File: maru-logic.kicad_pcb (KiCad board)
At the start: 2 copper layers, 182.9 x 111.8 mm, 190 parts, among them J1 USB-C, Q1 MMBT3904, Q10 MMBT3904, Q11 MMBT3904, Q12 MMBT3904, Q2 MMBT3904, Q3 MMBT3904, Q4 MMBT3904, Q5 MMBT3904, Q6 MMBT3904, Q7 MMBT3904, Q8 MMBT3904, Q9 MMBT3904, SW1 Push, SW2 Push, SW3 Push, SW4 Push, SW5 Push, SW6 Push, SW7 Push, U1 4011, U10 4011, U11 4011, U2 4011, U3 4011, U4 4011, U5 4011, U6 4011, U7 4011, U8 4011, U9 4011

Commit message: routing done
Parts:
- added C12: 100n, Capacitor_SMD:C_0402_1005Metric, F.Cu at (48.9, 76.8)
- added C3: 100n, Capacitor_SMD:C_0402_1005Metric, F.Cu at (79.5, 93.5)
- added C6: 100n, Capacitor_SMD:C_0402_1005Metric, F.Cu at (79.5, 69.6)
- added C9: 100n, Capacitor_SMD:C_0402_1005Metric, F.Cu at (79.5, 45.2)
- SW1, SW2, SW3, SW4, SW5, SW6, SW7: footprint mark:BUTTON_XKB_TS-1187A-B-A-B_C318884 -> mark:jlc_pushbutton_wrong_model
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- renumbered C8 to C10, C9 to C11, C2 to C13, C10 to C14, C11 to C15, C12 to C16, C13 to C17, C14 to C18, C15 to C19, C3 to C2, C6 to C7, C7 to C8, Q3 to Q1, Q7 to Q10, Q8 to Q11, Q10 to Q12, Q6 to Q2, Q9 to Q3, Q11 to Q4, Q12 to Q5, Q1 to Q6, Q2 to Q7, Q4 to Q8, Q5 to Q9, R2 to R1, R15 to R10, R16 to R11, R17 to R12, R25 to R13, R26 to R14, R27 to R15, R28 to R16, R29 to R17, R30 to R18, R43 to R19, R3 to R2, R44 to R20, R45 to R21, R46 to R22, R47 to R23, R48 to R24, R61 to R25, R62 to R26, R63 to R27, R64 to R28, R65 to R29, R1 to R3, R66 to R30, R73 to R31, R74 to R32, R75 to R33, R76 to R34, R77 to R35, R78 to R36, R79 to R37, R80 to R38, R81 to R39, R9 to R4, R82 to R40, R83 to R41, R84 to R42, R4 to R43, R5 to R44, R6 to R45, R7 to R46, R8 to R47, R18 to R48, R19 to R49, R10 to R5, R20 to R50, R21 to R51, R22 to R52, R23 to R53, R24 to R54, R31 to R55, R32 to R56, R33 to R57, R34 to R58, R35 to R59, R11 to R6, R36 to R60, R37 to R61, R38 to R62, R39 to R63, R40 to R64, R41 to R65, R42 to R66, R49 to R67, R50 to R68, R51 to R69, R12 to R7, R52 to R70, R53 to R71, R54 to R72, R55 to R73, R56 to R74, R57 to R75, R58 to R76, R59 to R77, R60 to R78, R67 to R79, R13 to R8, R68 to R80, R69 to R81, R70 to R82, R71 to R83, R72 to R84, R14 to R9, U3 to U2, U2 to U3, U5 to U4, U4 to U5
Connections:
- D1 pad 1: /Toggle Button 1/LEDs 1/LED drivers/LED1 -> /Output LEDs/LED_AND_X/LED array x5/LED1
- D10 pad 1: /Toggle Button 2/LEDs 1/LED drivers/LED5 -> /Output LEDs/LED_OR_X/LED array x5/LED5
- D11 pad 1: /Output LEDs/LED_AND_X/LED drivers/LED1 -> /Output LEDs/LED_XOR_X/LED array x5/LED1
- D12 pad 1: /Output LEDs/LED_AND_X/LED drivers/LED2 -> /Output LEDs/LED_XOR_X/LED array x5/LED2
- D13 pad 1: /Output LEDs/LED_AND_X/LED drivers/LED3 -> /Output LEDs/LED_XOR_X/LED array x5/LED3
- D14 pad 1: /Output LEDs/LED_AND_X/LED drivers/LED4 -> /Output LEDs/LED_XOR_X/LED array x5/LED4
- D15 pad 1: /Output LEDs/LED_AND_X/LED drivers/LED5 -> /Output LEDs/LED_XOR_X/LED array x5/LED5
- D16 pad 1: /Toggle Button 3/LEDs 1/LED drivers/LED1 -> /Output LEDs/LED_NOT_X/LED array x5/LED1
- D17 pad 1: /Toggle Button 3/LEDs 1/LED drivers/LED2 -> /Output LEDs/LED_NOT_X/LED array x5/LED2
- D18 pad 1: /Toggle Button 3/LEDs 1/LED drivers/LED3 -> /Output LEDs/LED_NOT_X/LED array x5/LED3
- D19 pad 1: /Toggle Button 3/LEDs 1/LED drivers/LED4 -> /Output LEDs/LED_NOT_X/LED array x5/LED4
- D2 pad 1: /Toggle Button 1/LEDs 1/LED drivers/LED2 -> /Output LEDs/LED_AND_X/LED array x5/LED2
- D20 pad 1: /Toggle Button 3/LEDs 1/LED drivers/LED5 -> /Output LEDs/LED_NOT_X/LED array x5/LED5
- D21 pad 1: /Toggle Button 4/LEDs 1/LED drivers/LED1 -> /Output LEDs/LED_ALL_X/LED array x5/LED1
- D22 pad 1: /Toggle Button 4/LEDs 1/LED drivers/LED2 -> /Output LEDs/LED_ALL_X/LED array x5/LED2
- D23 pad 1: /Toggle Button 4/LEDs 1/LED drivers/LED3 -> /Output LEDs/LED_ALL_X/LED array x5/LED3
- D24 pad 1: /Toggle Button 4/LEDs 1/LED drivers/LED4 -> /Output LEDs/LED_ALL_X/LED array x5/LED4
- D25 pad 1: /Toggle Button 4/LEDs 1/LED drivers/LED5 -> /Output LEDs/LED_ALL_X/LED array x5/LED5
- D26 pad 1: /Output LEDs/LED_OR_X/LED drivers/LED1 -> /Toggle Button 1/LEDs 1/LED array x5/LED1
- D27 pad 1: /Output LEDs/LED_OR_X/LED drivers/LED2 -> /Toggle Button 1/LEDs 1/LED array x5/LED2
- D28 pad 1: /Output LEDs/LED_OR_X/LED drivers/LED3 -> /Toggle Button 1/LEDs 1/LED array x5/LED3
- D29 pad 1: /Output LEDs/LED_OR_X/LED drivers/LED4 -> /Toggle Button 1/LEDs 1/LED array x5/LED4
- D3 pad 1: /Toggle Button 1/LEDs 1/LED drivers/LED3 -> /Output LEDs/LED_AND_X/LED array x5/LED3
- D30 pad 1: /Output LEDs/LED_OR_X/LED drivers/LED5 -> /Toggle Button 1/LEDs 1/LED array x5/LED5
- D31 pad 1: /Toggle Button 5/LEDs 1/LED drivers/LED1 -> /Toggle Button 2/LEDs 1/LED array x5/LED1
- D32 pad 1: /Toggle Button 5/LEDs 1/LED drivers/LED2 -> /Toggle Button 2/LEDs 1/LED array x5/LED2
- D33 pad 1: /Toggle Button 5/LEDs 1/LED drivers/LED3 -> /Toggle Button 2/LEDs 1/LED array x5/LED3
- D34 pad 1: /Toggle Button 5/LEDs 1/LED drivers/LED4 -> /Toggle Button 2/LEDs 1/LED array x5/LED4
- D35 pad 1: /Toggle Button 5/LEDs 1/LED drivers/LED5 -> /Toggle Button 2/LEDs 1/LED array x5/LED5
- D36 pad 1: /Toggle Button 6/LEDs 1/LED drivers/LED1 -> /Toggle Button 3/LEDs 1/LED array x5/LED1
- D37 pad 1: /Toggle Button 6/LEDs 1/LED drivers/LED2 -> /Toggle Button 3/LEDs 1/LED array x5/LED2
- D38 pad 1: /Toggle Button 6/LEDs 1/LED drivers/LED3 -> /Toggle Button 3/LEDs 1/LED array x5/LED3
- D39 pad 1: /Toggle Button 6/LEDs 1/LED drivers/LED4 -> /Toggle Button 3/LEDs 1/LED array x5/LED4
- D4 pad 1: /Toggle Button 1/LEDs 1/LED drivers/LED4 -> /Output LEDs/LED_AND_X/LED array x5/LED4
- D40 pad 1: /Toggle Button 6/LEDs 1/LED drivers/LED5 -> /Toggle Button 3/LEDs 1/LED array x5/LED5
- D41 pad 1: /Output LEDs/LED_XOR_X/LED drivers/LED1 -> /Toggle Button 4/LEDs 1/LED array x5/LED1
- D42 pad 1: /Output LEDs/LED_XOR_X/LED drivers/LED2 -> /Toggle Button 4/LEDs 1/LED array x5/LED2
- D43 pad 1: /Output LEDs/LED_XOR_X/LED drivers/LED3 -> /Toggle Button 4/LEDs 1/LED array x5/LED3
- D44 pad 1: /Output LEDs/LED_XOR_X/LED drivers/LED4 -> /Toggle Button 4/LEDs 1/LED array x5/LED4
- D45 pad 1: /Output LEDs/LED_XOR_X/LED drivers/LED5 -> /Toggle Button 4/LEDs 1/LED array x5/LED5
- D46 pad 1: /Toggle Button 7/LEDs 1/LED drivers/LED1 -> /Toggle Button 5/LEDs 1/LED array x5/LED1
- D47 pad 1: /Toggle Button 7/LEDs 1/LED drivers/LED2 -> /Toggle Button 5/LEDs 1/LED array x5/LED2
- D48 pad 1: /Toggle Button 7/LEDs 1/LED drivers/LED3 -> /Toggle Button 5/LEDs 1/LED array x5/LED3
- D49 pad 1: /Toggle Button 7/LEDs 1/LED drivers/LED4 -> /Toggle Button 5/LEDs 1/LED array x5/LED4
- D5 pad 1: /Toggle Button 1/LEDs 1/LED drivers/LED5 -> /Output LEDs/LED_AND_X/LED array x5/LED5
- D50 pad 1: /Toggle Button 7/LEDs 1/LED drivers/LED5 -> /Toggle Button 5/LEDs 1/LED array x5/LED5
- D51 pad 1: /Output LEDs/LED_NOT_X/LED drivers/LED1 -> /Toggle Button 6/LEDs 1/LED array x5/LED1
- D52 pad 1: /Output LEDs/LED_NOT_X/LED drivers/LED2 -> /Toggle Button 6/LEDs 1/LED array x5/LED2
- D53 pad 1: /Output LEDs/LED_NOT_X/LED drivers/LED3 -> /Toggle Button 6/LEDs 1/LED array x5/LED3
- D54 pad 1: /Output LEDs/LED_NOT_X/LED drivers/LED4 -> /Toggle Button 6/LEDs 1/LED array x5/LED4
- D55 pad 1: /Output LEDs/LED_NOT_X/LED drivers/LED5 -> /Toggle Button 6/LEDs 1/LED array x5/LED5
- D56 pad 1: /Output LEDs/LED_ALL_X/LED drivers/LED1 -> /Toggle Button 7/LEDs 1/LED array x5/LED1
- D57 pad 1: /Output LEDs/LED_ALL_X/LED drivers/LED2 -> /Toggle Button 7/LEDs 1/LED array x5/LED2
- D58 pad 1: /Output LEDs/LED_ALL_X/LED drivers/LED3 -> /Toggle Button 7/LEDs 1/LED array x5/LED3
- D59 pad 1: /Output LEDs/LED_ALL_X/LED drivers/LED4 -> /Toggle Button 7/LEDs 1/LED array x5/LED4
- D6 pad 1: /Toggle Button 2/LEDs 1/LED drivers/LED1 -> /Output LEDs/LED_OR_X/LED array x5/LED1
- D60 pad 1: /Output LEDs/LED_ALL_X/LED drivers/LED5 -> /Toggle Button 7/LEDs 1/LED array x5/LED5
- D7 pad 1: /Toggle Button 2/LEDs 1/LED drivers/LED2 -> /Output LEDs/LED_OR_X/LED array x5/LED2
- D8 pad 1: /Toggle Button 2/LEDs 1/LED drivers/LED3 -> /Output LEDs/LED_OR_X/LED array x5/LED3
- D9 pad 1: /Toggle Button 2/LEDs 1/LED drivers/LED4 -> /Output LEDs/LED_OR_X/LED array x5/LED4
- R14 pad 1: /Output LEDs/LED_AND_X/LED drivers/LED1 -> /Output LEDs/LED_AND_X/LED array x5/LED1
- R15 pad 1: /Output LEDs/LED_AND_X/LED drivers/LED2 -> /Output LEDs/LED_AND_X/LED array x5/LED2
- R16 pad 1: /Output LEDs/LED_AND_X/LED drivers/LED3 -> /Output LEDs/LED_AND_X/LED array x5/LED3
- R17 pad 1: /Output LEDs/LED_AND_X/LED drivers/LED4 -> /Output LEDs/LED_AND_X/LED array x5/LED4
- R18 pad 1: /Output LEDs/LED_AND_X/LED drivers/LED5 -> /Output LEDs/LED_AND_X/LED array x5/LED5
- R20 pad 1: /Output LEDs/LED_OR_X/LED drivers/LED1 -> /Output LEDs/LED_OR_X/LED array x5/LED1
- R21 pad 1: /Output LEDs/LED_OR_X/LED drivers/LED2 -> /Output LEDs/LED_OR_X/LED array x5/LED2
- R22 pad 1: /Output LEDs/LED_OR_X/LED drivers/LED3 -> /Output LEDs/LED_OR_X/LED array x5/LED3
- R23 pad 1: /Output LEDs/LED_OR_X/LED drivers/LED4 -> /Output LEDs/LED_OR_X/LED array x5/LED4
- R24 pad 1: /Output LEDs/LED_OR_X/LED drivers/LED5 -> /Output LEDs/LED_OR_X/LED array x5/LED5
- R26 pad 1: /Output LEDs/LED_XOR_X/LED drivers/LED1 -> /Output LEDs/LED_XOR_X/LED array x5/LED1
- R27 pad 1: /Output LEDs/LED_XOR_X/LED drivers/LED2 -> /Output LEDs/LED_XOR_X/LED array x5/LED2
- R28 pad 1: /Output LEDs/LED_XOR_X/LED drivers/LED3 -> /Output LEDs/LED_XOR_X/LED array x5/LED3
- R29 pad 1: /Output LEDs/LED_XOR_X/LED drivers/LED4 -> /Output LEDs/LED_XOR_X/LED array x5/LED4
- R30 pad 1: /Output LEDs/LED_XOR_X/LED drivers/LED5 -> /Output LEDs/LED_XOR_X/LED array x5/LED5
- R32 pad 1: /Output LEDs/LED_NOT_X/LED drivers/LED1 -> /Output LEDs/LED_NOT_X/LED array x5/LED1
- R33 pad 1: /Output LEDs/LED_NOT_X/LED drivers/LED2 -> /Output LEDs/LED_NOT_X/LED array x5/LED2
- R34 pad 1: /Output LEDs/LED_NOT_X/LED drivers/LED3 -> /Output LEDs/LED_NOT_X/LED array x5/LED3
- R35 pad 1: /Output LEDs/LED_NOT_X/LED drivers/LED4 -> /Output LEDs/LED_NOT_X/LED array x5/LED4
- R36 pad 1: /Output LEDs/LED_NOT_X/LED drivers/LED5 -> /Output LEDs/LED_NOT_X/LED array x5/LED5
- R38 pad 1: /Output LEDs/LED_ALL_X/LED drivers/LED1 -> /Output LEDs/LED_ALL_X/LED array x5/LED1
- R39 pad 1: /Output LEDs/LED_ALL_X/LED drivers/LED2 -> /Output LEDs/LED_ALL_X/LED array x5/LED2
- R40 pad 1: /Output LEDs/LED_ALL_X/LED drivers/LED3 -> /Output LEDs/LED_ALL_X/LED array x5/LED3
- R41 pad 1: /Output LEDs/LED_ALL_X/LED drivers/LED4 -> /Output LEDs/LED_ALL_X/LED array x5/LED4
- R42 pad 1: /Output LEDs/LED_ALL_X/LED drivers/LED5 -> /Output LEDs/LED_ALL_X/LED array x5/LED5
- R44 pad 1: /Toggle Button 1/LEDs 1/LED drivers/LED1 -> /Toggle Button 1/LEDs 1/LED array x5/LED1
- R45 pad 1: /Toggle Button 1/LEDs 1/LED drivers/LED2 -> /Toggle Button 1/LEDs 1/LED array x5/LED2
- R46 pad 1: /Toggle Button 1/LEDs 1/LED drivers/LED3 -> /Toggle Button 1/LEDs 1/LED array x5/LED3
- R47 pad 1: /Toggle Button 1/LEDs 1/LED drivers/LED4 -> /Toggle Button 1/LEDs 1/LED array x5/LED4
- R48 pad 1: /Toggle Button 1/LEDs 1/LED drivers/LED5 -> /Toggle Button 1/LEDs 1/LED array x5/LED5
- R50 pad 1: /Toggle Button 2/LEDs 1/LED drivers/LED1 -> /Toggle Button 2/LEDs 1/LED array x5/LED1
- R51 pad 1: /Toggle Button 2/LEDs 1/LED drivers/LED2 -> /Toggle Button 2/LEDs 1/LED array x5/LED2
- R52 pad 1: /Toggle Button 2/LEDs 1/LED drivers/LED3 -> /Toggle Button 2/LEDs 1/LED array x5/LED3
- R53 pad 1: /Toggle Button 2/LEDs 1/LED drivers/LED4 -> /Toggle Button 2/LEDs 1/LED array x5/LED4
- R54 pad 1: /Toggle Button 2/LEDs 1/LED drivers/LED5 -> /Toggle Button 2/LEDs 1/LED array x5/LED5
- R56 pad 1: /Toggle Button 3/LEDs 1/LED drivers/LED1 -> /Toggle Button 3/LEDs 1/LED array x5/LED1
- R57 pad 1: /Toggle Button 3/LEDs 1/LED drivers/LED2 -> /Toggle Button 3/LEDs 1/LED array x5/LED2
- R58 pad 1: /Toggle Button 3/LEDs 1/LED drivers/LED3 -> /Toggle Button 3/LEDs 1/LED array x5/LED3
- R59 pad 1: /Toggle Button 3/LEDs 1/LED drivers/LED4 -> /Toggle Button 3/LEDs 1/LED array x5/LED4
- R60 pad 1: /Toggle Button 3/LEDs 1/LED drivers/LED5 -> /Toggle Button 3/LEDs 1/LED array x5/LED5
- R62 pad 1: /Toggle Button 4/LEDs 1/LED drivers/LED1 -> /Toggle Button 4/LEDs 1/LED array x5/LED1
- R63 pad 1: /Toggle Button 4/LEDs 1/LED drivers/LED2 -> /Toggle Button 4/LEDs 1/LED array x5/LED2
- R64 pad 1: /Toggle Button 4/LEDs 1/LED drivers/LED3 -> /Toggle Button 4/LEDs 1/LED array x5/LED3
- R65 pad 1: /Toggle Button 4/LEDs 1/LED drivers/LED4 -> /Toggle Button 4/LEDs 1/LED array x5/LED4
- R66 pad 1: /Toggle Button 4/LEDs 1/LED drivers/LED5 -> /Toggle Button 4/LEDs 1/LED array x5/LED5
- R68 pad 1: /Toggle Button 5/LEDs 1/LED drivers/LED1 -> /Toggle Button 5/LEDs 1/LED array x5/LED1
- R69 pad 1: /Toggle Button 5/LEDs 1/LED drivers/LED2 -> /Toggle Button 5/LEDs 1/LED array x5/LED2
- R70 pad 1: /Toggle Button 5/LEDs 1/LED drivers/LED3 -> /Toggle Button 5/LEDs 1/LED array x5/LED3
- R71 pad 1: /Toggle Button 5/LEDs 1/LED drivers/LED4 -> /Toggle Button 5/LEDs 1/LED array x5/LED4
- R72 pad 1: /Toggle Button 5/LEDs 1/LED drivers/LED5 -> /Toggle Button 5/LEDs 1/LED array x5/LED5
- R74 pad 1: /Toggle Button 6/LEDs 1/LED drivers/LED1 -> /Toggle Button 6/LEDs 1/LED array x5/LED1
- R75 pad 1: /Toggle Button 6/LEDs 1/LED drivers/LED2 -> /Toggle Button 6/LEDs 1/LED array x5/LED2
- R76 pad 1: /Toggle Button 6/LEDs 1/LED drivers/LED3 -> /Toggle Button 6/LEDs 1/LED array x5/LED3
- R77 pad 1: /Toggle Button 6/LEDs 1/LED drivers/LED4 -> /Toggle Button 6/LEDs 1/LED array x5/LED4
- R78 pad 1: /Toggle Button 6/LEDs 1/LED drivers/LED5 -> /Toggle Button 6/LEDs 1/LED array x5/LED5
- R80 pad 1: /Toggle Button 7/LEDs 1/LED drivers/LED1 -> /Toggle Button 7/LEDs 1/LED array x5/LED1
- R81 pad 1: /Toggle Button 7/LEDs 1/LED drivers/LED2 -> /Toggle Button 7/LEDs 1/LED array x5/LED2
- R82 pad 1: /Toggle Button 7/LEDs 1/LED drivers/LED3 -> /Toggle Button 7/LEDs 1/LED array x5/LED3
- R83 pad 1: /Toggle Button 7/LEDs 1/LED drivers/LED4 -> /Toggle Button 7/LEDs 1/LED array x5/LED4
- R84 pad 1: /Toggle Button 7/LEDs 1/LED drivers/LED5 -> /Toggle Button 7/LEDs 1/LED array x5/LED5
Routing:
- net /Output LEDs/LED_ALL_X/LED array x5/LED5: track 0.00 -> 234.6 mm, vias 0 -> 2
- net /Output LEDs/LED_ALL_X/LED array x5/LED4: track 0.00 -> 226.9 mm, vias 0 -> 2
- net /Output LEDs/LED_ALL_X/LED array x5/LED2: track 0.00 -> 215.9 mm, vias 0 -> 2
- net /Output LEDs/LED_ALL_X/LED array x5/LED3: track 0.00 -> 215.7 mm, vias 0 -> 2
- net VDD: track 69.2 -> 284.4 mm, vias 12 -> 20
- net /Output LEDs/LED_ALL_X/LED array x5/LED1: track 0.00 -> 199.9 mm, vias 0 -> 2
- net /Output LEDs/LED_NOT_X/LED array x5/LED5: track 0.00 -> 126.4 mm, vias 0 -> 2
- net /Output LEDs/LED_NOT_X/LED array x5/LED4: track 0.00 -> 120.3 mm, vias 0 -> 2
- net /Output LEDs/LED_AND_X/LED array x5/LED5: track 0.00 -> 112.7 mm, vias 0 -> 2
- net /Output LEDs/LED_OR_X/LED array x5/LED5: track 0.00 -> 110.0 mm, vias 0 -> 2
- net /Output LEDs/LED_XOR_X/LED array x5/LED5: track 0.00 -> 109.0 mm, vias 0 -> 2
- net /Output LEDs/LED_AND_X/LED array x5/LED4: track 0.00 -> 107.0 mm, vias 0 -> 2
- net /Output LEDs/LED_OR_X/LED array x5/LED4: track 0.00 -> 104.5 mm, vias 0 -> 2
- net VDDF: track 0.00 -> 102.9 mm
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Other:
- board size 182.9 x 111.8 mm -> 231.1 x 132.1 mm
- board text added: "AND"
- board text added: "NOT"
- board text added: "OR"
- board text added: "XOR"

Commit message: ready to order
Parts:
- added C12: 100n, Capacitor_SMD:C_0402_1005Metric, F.Cu at (79.2, 104.1)
- added C16: 100n, Capacitor_SMD:C_0402_1005Metric, F.Cu at (79.4, 80.3)
- added C4: 100n, Capacitor_SMD:C_0402_1005Metric, F.Cu at (88.9, 61.0)
- added C8: 100n, Capacitor_SMD:C_0402_1005Metric, F.Cu at (79.4, 55.9)
- added H1: JLC, mark:JLCPCB_ToolingHole_1152_1300_1400_1650, F.Cu at (256.5, 114.3)
- added H2: JLC, mark:JLCPCB_ToolingHole_1152_1300_1400_1650, F.Cu at (48.3, 111.8)
- added H3: MountingHole, MountingHole:MountingHole_2.2mm_M2_ISO7380, F.Cu at (50.8, 15.2)
- added H4: MountingHole, MountingHole:MountingHole_2.2mm_M2_ISO7380, F.Cu at (50.8, 116.8)
- added H5: JLC, mark:JLCPCB_ToolingHole_1152_1300_1400_1650, F.Cu at (256.5, 17.8)
- added H6: JLC, mark:JLCPCB_ToolingHole_1152_1300_1400_1650, F.Cu at (48.3, 20.3)
- added H7: MountingHole, MountingHole:MountingHole_2.2mm_M2_ISO7380, F.Cu at (91.4, 15.2)
- added H8: MountingHole, MountingHole:MountingHole_2.2mm_M2_ISO7380, F.Cu at (91.4, 116.8)
- D1, D10, D11, D12, D13, D14, D15, D16, D17, D18, D19, D2, D20, D21, D22, D23, D24, D25, D26, D27, D28, D29, D3, D30, D31, D32, D33, D34, D35, D36, D37, D38, D39, D4, D40, D41, D42, D43, D44, D45, D46, D47, D48, D49, D5, D50, D51, D52, D53, D54, D55, D56, D57, D58, D59, D6, D60, D7, D8, D9: footprint LED_SMD:LED_0603_1608Metric -> mark:LED_0603_1608Metric_no_silk
- SW1, SW2, SW3, SW4, SW5, SW6, SW7: footprint mark:jlc_pushbutton_wrong_model -> mark:jlc_pushbutton
- U1, U10, U11, U2, U3, U4, U5, U6, U7, U8, U9: value 4011 -> 4093
- moved R4 13.4 mm to (52.1, 64.1), turned to -90 degrees
- moved J1 12.7 mm to (45.8, 66.0)
- moved R5 11.8 mm to (52.1, 67.9), turned to 90 degrees
- moved C15 11.4 mm to (52.7, 66.0)
- renumbered C8 to C10, C9 to C11, C10 to C13, C11 to C14, C12 to C15, C13 to C17, C14 to C18, C15 to C19, C16 to C20, C17 to C21, C18 to C22, C19 to C23, C4 to C5, C5 to C6, C6 to C7, C7 to C9, R3 to R1, R4 to R2, R5 to R3, R1 to R4, R2 to R5
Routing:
- net VSS: track 117.5 -> 167.4 mm, vias 37 -> 43
- net VDDF: track 102.9 -> 143.2 mm, vias 0 -> 2
- net VDD: track 284.4 -> 303.8 mm
- net /Output LEDs/LED_ALL_X/LED array x5/LED5: track 234.6 -> 215.4 mm
- net /Output LEDs/LED_ALL_X/LED array x5/LED4: track 226.9 -> 210.4 mm
- net /Output LEDs/LED_ALL_X/LED array x5/LED2: track 215.9 -> 200.1 mm
- net /Output LEDs/LED_AND_X/LED array x5/LED2: track 98.7 -> 85.0 mm
- net /Output LEDs/LED_AND_X/LED array x5/LED3: track 102.8 -> 89.1 mm
- net /Output LEDs/LED_AND_X/LED array x5/LED1: track 92.4 -> 79.9 mm
- net /Output LEDs/LED_ALL_X/LED array x5/LED3: track 215.7 -> 205.2 mm
- net /Output LEDs/LED_NOT_X/LED array x5/LED5: track 126.4 -> 116.1 mm
- net /Output LEDs/LED_XOR_X/LED array x5/LED3: track 97.3 -> 88.1 mm
- net /Output LEDs/LED_XOR_X/LED array x5/LED2: track 92.8 -> 83.6 mm
- net /Output LEDs/LED_XOR_X/LED array x5/LED1: track 86.4 -> 77.7 mm
- net /Output LEDs/LED_NOT_X/LED array x5/LED4: track 120.3 -> 111.6 mm
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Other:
- board size 231.1 x 132.1 mm -> 223.5 x 116.8 mm
- board text added: "Routing is intentionally shit, so I can use unpopulated boards to study crosstalk"

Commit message: pre-re-layout
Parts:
- removed C1, C10, C13, C17, C18, C19, C2, C20, C21, C22, C23, C5, C6, C9: 100n, Capacitor_SMD:C_0402_1005Metric
- removed D1, D10, D11, D12, D13, D14, D15, D16, D17, D18, D19, D2, D20, D21, D22, D23, D24, D25, D26, D27, D28, D29, D3, D30, D31, D32, D33, D34, D35, D36, D37, D38, D39, D4, D40, D41, D42, D43, D44, D45, D46, D47, D48, D49, D5, D50, D51, D52, D53, D54, D55, D56, D57, D58, D59, D6, D60, D7, D8, D9: White, mark:LED_0603_1608Metric_no_silk
- removed Q1, Q10, Q11, Q12, Q2, Q3, Q4, Q5, Q6, Q7, Q8, Q9: MMBT3904, Package_TO_SOT_SMD:SOT-23
- removed R1, R13, R19, R2, R25, R3, R31, R37, R43, R49, R55, R61, R67, R73, R79: 5.1k, Resistor_SMD:R_0402_1005Metric
- removed R10, R11, R12, R6, R7, R8, R9: 100k, Resistor_SMD:R_0402_1005Metric
- removed R14, R15, R16, R17, R18, R20, R21, R22, R23, R24, R26, R27, R28, R29, R30, R32, R33, R34, R35, R36, R38, R39, R40, R41, R42, R44, R45, R46, R47, R48, R50, R51, R52, R53, R54, R56, R57, R58, R59, R60, R62, R63, R64, R65, R66, R68, R69, R70, R71, R72, R74, R75, R76, R77, R78, R80, R81, R82, R83, R84: 200, Resistor_SMD:R_0402_1005Metric
- removed U10, U11, U5, U6, U7, U8, U9: 4093, Package_SO:SOIC-14_3.9x8.7mm_P1.27mm
- added C10001: 100n, Capacitor_SMD:C_0402_1005Metric, F.Cu at (120.8, 189.8)
- added C10101: 100n, Capacitor_SMD:C_0402_1005Metric, F.Cu at (87.9, 221.5)
- added C10201: 100n, Capacitor_SMD:C_0402_1005Metric, F.Cu at (71.5, 232.1)
- added C10301: 100n, Capacitor_SMD:C_0402_1005Metric, F.Cu at (137.2, 179.3)
- added C1101: 100n, Capacitor_SMD:C_0402_1005Metric, F.Cu at (69.6, 49.8)
- added C1102: 1n, Capacitor_SMD:C_0402_1005Metric, F.Cu at (58.4, 55.1)
- added C1103: 1n, Capacitor_SMD:C_0402_1005Metric, F.Cu at (57.7, 50.8)
- added C1104: 1n, Capacitor_SMD:C_0402_1005Metric, F.Cu at (57.7, 53.4)
- added C1301: 100n, Capacitor_SMD:C_0402_1005Metric, F.Cu at (69.6, 62.5)
- added C1302: 1n, Capacitor_SMD:C_0402_1005Metric, F.Cu at (58.4, 67.8)
- added C1303: 1n, Capacitor_SMD:C_0402_1005Metric, F.Cu at (57.7, 63.5)
- added C1304: 1n, Capacitor_SMD:C_0402_1005Metric, F.Cu at (57.7, 66.1)
- added C1501: 100n, Capacitor_SMD:C_0402_1005Metric, F.Cu at (69.6, 75.2)
- added C1502: 1n, Capacitor_SMD:C_0402_1005Metric, F.Cu at (58.4, 80.5)
- added C1503: 1n, Capacitor_SMD:C_0402_1005Metric, F.Cu at (57.7, 76.2)
- added C1504: 1n, Capacitor_SMD:C_0402_1005Metric, F.Cu at (57.7, 78.8)
- added C1701: 100n, Capacitor_SMD:C_0402_1005Metric, F.Cu at (137.2, 242.6)
- added C1801: 100n, Capacitor_SMD:C_0402_1005Metric, F.Cu at (120.8, 200.4)
- added C1901: 100n, Capacitor_SMD:C_0402_1005Metric, F.Cu at (120.8, 210.9)
- added C2001: 100n, Capacitor_SMD:C_0402_1005Metric, F.Cu at (87.9, 200.4)
- added C201: 100n, Capacitor_SMD:C_0402_1005Metric, F.Cu at (69.6, 24.4)
- added C202: 1n, Capacitor_SMD:C_0402_1005Metric, F.Cu at (58.4, 29.7)
- added C203: 1n, Capacitor_SMD:C_0402_1005Metric, F.Cu at (57.7, 25.4)
- added C204: 1n, Capacitor_SMD:C_0402_1005Metric, F.Cu at (57.7, 28.0)
- added C2101: 100n, Capacitor_SMD:C_0402_1005Metric, F.Cu at (153.6, 168.7)
- added C2201: 100n, Capacitor_SMD:C_0402_1005Metric, F.Cu at (71.5, 210.9)
- added C2301: 100n, Capacitor_SMD:C_0402_1005Metric, F.Cu at (137.2, 158.2)
- added C2401: 100n, Capacitor_SMD:C_0402_1005Metric, F.Cu at (120.8, 168.7)
- added C2501: 100n, Capacitor_SMD:C_0402_1005Metric, F.Cu at (55.1, 232.1)
- added C2601: 100n, Capacitor_SMD:C_0402_1005Metric, F.Cu at (71.5, 158.2)
- added C2701: 100n, Capacitor_SMD:C_0402_1005Metric, F.Cu at (104.3, 158.2)
- added C2801: 100n, Capacitor_SMD:C_0402_1005Metric, F.Cu at (71.5, 168.7)
- added C2901: 100n, Capacitor_SMD:C_0402_1005Metric, F.Cu at (55.1, 168.7)
- added C3001: 100n, Capacitor_SMD:C_0402_1005Metric, F.Cu at (55.1, 179.3)
- added C3201: 100n, Capacitor_SMD:C_0402_1005Metric, F.Cu at (71.5, 179.3)
- added C3301: 100n, Capacitor_SMD:C_0402_1005Metric, F.Cu at (87.9, 158.2)
- added C3401: 100n, Capacitor_SMD:C_0402_1005Metric, F.Cu at (55.1, 221.5)
- added C3501: 100n, Capacitor_SMD:C_0402_1005Metric, F.Cu at (71.5, 200.4)
- added C3601: 100n, Capacitor_SMD:C_0402_1005Metric, F.Cu at (55.1, 242.6)
- added C3701: 100n, Capacitor_SMD:C_0402_1005Metric, F.Cu at (120.8, 158.2)
- added C3801: 100n, Capacitor_SMD:C_0402_1005Metric, F.Cu at (87.9, 189.8)
- added C3901: 100n, Capacitor_SMD:C_0402_1005Metric, F.Cu at (55.1, 200.4)
- added C4001: 100n, Capacitor_SMD:C_0402_1005Metric, F.Cu at (55.1, 189.8)
- added C401: 100n, Capacitor_SMD:C_0402_1005Metric, F.Cu at (104.3, 210.9)
- added C4301: 100n, Capacitor_SMD:C_0402_1005Metric, F.Cu at (170.0, 179.3)
- added C4501: 100n, Capacitor_SMD:C_0402_1005Metric, F.Cu at (186.4, 189.8)
- added C4601: 100n, Capacitor_SMD:C_0402_1005Metric, F.Cu at (219.3, 158.2)
- added C4701: 100n, Capacitor_SMD:C_0402_1005Metric, F.Cu at (170.0, 200.4)
- added C4801: 100n, Capacitor_SMD:C_0402_1005Metric, F.Cu at (137.2, 232.1)
- added C4901: 100n, Capacitor_SMD:C_0402_1005Metric, F.Cu at (202.8, 179.3)
- added C5001: 100n, Capacitor_SMD:C_0402_1005Metric, F.Cu at (153.6, 221.5)
- added C501: 100n, Capacitor_SMD:C_0402_1005Metric, F.Cu at (69.6, 87.9)
- added C502: 1n, Capacitor_SMD:C_0402_1005Metric, F.Cu at (58.4, 93.2)
- added C503: 1n, Capacitor_SMD:C_0402_1005Metric, F.Cu at (57.7, 88.9)
- added C504: 1n, Capacitor_SMD:C_0402_1005Metric, F.Cu at (57.7, 91.5)
- added C5101: 100n, Capacitor_SMD:C_0402_1005Metric, F.Cu at (120.8, 221.5)
- added C5201: 100n, Capacitor_SMD:C_0402_1005Metric, F.Cu at (153.6, 210.9)
- added C5301: 100n, Capacitor_SMD:C_0402_1005Metric, F.Cu at (87.9, 168.7)
- added C5501: 100n, Capacitor_SMD:C_0402_1005Metric, F.Cu at (120.8, 232.1)
- added C5601: 100n, Capacitor_SMD:C_0402_1005Metric, F.Cu at (186.4, 168.7)
- added C5701: 100n, Capacitor_SMD:C_0402_1005Metric, F.Cu at (137.2, 221.5)
- added C5801: 100n, Capacitor_SMD:C_0402_1005Metric, F.Cu at (153.6, 200.4)
- added C5901: 100n, Capacitor_SMD:C_0402_1005Metric, F.Cu at (202.8, 158.2)
- added C6101: 100n, Capacitor_SMD:C_0402_1005Metric, F.Cu at (137.2, 200.4)
- added C6201: 100n, Capacitor_SMD:C_0402_1005Metric, F.Cu at (71.5, 242.6)
- added C6301: 100n, Capacitor_SMD:C_0402_1005Metric, F.Cu at (186.4, 158.2)
- added C6401: 100n, Capacitor_SMD:C_0402_1005Metric, F.Cu at (170.0, 168.7)
- added C6501: 100n, Capacitor_SMD:C_0402_1005Metric, F.Cu at (104.3, 232.1)
- added C6701: 100n, Capacitor_SMD:C_0402_1005Metric, F.Cu at (87.9, 179.3)
- added C6801: 100n, Capacitor_SMD:C_0402_1005Metric, F.Cu at (55.1, 158.2)
- added C6901: 100n, Capacitor_SMD:C_0402_1005Metric, F.Cu at (104.3, 168.7)
- added C7001: 100n, Capacitor_SMD:C_0402_1005Metric, F.Cu at (71.5, 189.8)
- added C701: 100n, Capacitor_SMD:C_0402_1005Metric, F.Cu at (69.6, 100.6)
- added C702: 1n, Capacitor_SMD:C_0402_1005Metric, F.Cu at (58.4, 105.9)
- added C703: 1n, Capacitor_SMD:C_0402_1005Metric, F.Cu at (57.7, 101.6)
- added C704: 1n, Capacitor_SMD:C_0402_1005Metric, F.Cu at (57.7, 104.2)
- added C7101: 100n, Capacitor_SMD:C_0402_1005Metric, F.Cu at (55.1, 210.9)
- added C7401: 100n, Capacitor_SMD:C_0402_1005Metric, F.Cu at (120.8, 242.6)
- added C7501: 100n, Capacitor_SMD:C_0402_1005Metric, F.Cu at (170.0, 189.8)
- added C7601: 100n, Capacitor_SMD:C_0402_1005Metric, F.Cu at (202.8, 168.7)
- added C7701: 100n, Capacitor_SMD:C_0402_1005Metric, F.Cu at (186.4, 179.3)
- added C7801: 100n, Capacitor_SMD:C_0402_1005Metric, F.Cu at (137.2, 210.9)
- added C8001: 100n, Capacitor_SMD:C_0402_1005Metric, F.Cu at (153.6, 189.8)
- added C8101: 100n, Capacitor_SMD:C_0402_1005Metric, F.Cu at (104.3, 242.6)
- added C8501: 100n, Capacitor_SMD:C_0402_1005Metric, F.Cu at (87.9, 210.9)
- added C8601: 100n, Capacitor_SMD:C_0402_1005Metric, F.Cu at (120.8, 179.3)
- added C8701: 100n, Capacitor_SMD:C_0402_1005Metric, F.Cu at (71.5, 221.5)
- added C8801: 100n, Capacitor_SMD:C_0402_1005Metric, F.Cu at (104.3, 189.8)
- added C8901: 100n, Capacitor_SMD:C_0402_1005Metric, F.Cu at (137.2, 168.7)
- added C9001: 100n, Capacitor_SMD:C_0402_1005Metric, F.Cu at (104.3, 179.3)
- added C901: 100n, Capacitor_SMD:C_0402_1005Metric, F.Cu at (69.6, 37.1)
- added C902: 1n, Capacitor_SMD:C_0402_1005Metric, F.Cu at (58.4, 42.4)
- added C903: 1n, Capacitor_SMD:C_0402_1005Metric, F.Cu at (57.7, 38.1)
- added C904: 1n, Capacitor_SMD:C_0402_1005Metric, F.Cu at (57.7, 40.7)
- added C9201: 100n, Capacitor_SMD:C_0402_1005Metric, F.Cu at (153.6, 179.3)
- added C9301: 100n, Capacitor_SMD:C_0402_1005Metric, F.Cu at (104.3, 221.5)
- added C9401: 100n, Capacitor_SMD:C_0402_1005Metric, F.Cu at (87.9, 232.1)
- added C9501: 100n, Capacitor_SMD:C_0402_1005Metric, F.Cu at (170.0, 158.2)
- added C9601: 100n, Capacitor_SMD:C_0402_1005Metric, F.Cu at (87.9, 242.6)
- added C9701: 100n, Capacitor_SMD:C_0402_1005Metric, F.Cu at (137.2, 189.8)
- added C9801: 100n, Capacitor_SMD:C_0402_1005Metric, F.Cu at (104.3, 200.4)
- added C9901: 100n, Capacitor_SMD:C_0402_1005Metric, F.Cu at (153.6, 158.2)
- added D10001: White, mark:LED_0603_1608Metric_no_silk, F.Cu at (117.3, 190.1)
- added D10101: White, mark:LED_0603_1608Metric_no_silk, F.Cu at (84.5, 221.8)
- added D10201: White, mark:LED_0603_1608Metric_no_silk, F.Cu at (68.0, 232.3)
- added D10301: White, mark:LED_0603_1608Metric_no_silk, F.Cu at (133.7, 179.5)
- added D1701: White, mark:LED_0603_1608Metric_no_silk, F.Cu at (133.7, 242.9)
- added D1801: White, mark:LED_0603_1608Metric_no_silk, F.Cu at (117.3, 200.7)
- added D1901: White, mark:LED_0603_1608Metric_no_silk, F.Cu at (117.3, 211.2)
- added D2001: White, mark:LED_0603_1608Metric_no_silk, F.Cu at (84.5, 200.7)
- added D2101: White, mark:LED_0603_1608Metric_no_silk, F.Cu at (150.2, 169.0)
- added D2201: White, mark:LED_0603_1608Metric_no_silk, F.Cu at (68.0, 211.2)
- added D2301: White, mark:LED_0603_1608Metric_no_silk, F.Cu at (133.7, 158.4)
- added D2401: White, mark:LED_0603_1608Metric_no_silk, F.Cu at (117.3, 169.0)
- added D2501: White, mark:LED_0603_1608Metric_no_silk, F.Cu at (51.6, 232.3)
- added D2601: White, mark:LED_0603_1608Metric_no_silk, F.Cu at (68.0, 158.4)
- added D2701: White, mark:LED_0603_1608Metric_no_silk, F.Cu at (100.9, 158.4)
- added D2801: White, mark:LED_0603_1608Metric_no_silk, F.Cu at (68.0, 169.0)
- added D2901: White, mark:LED_0603_1608Metric_no_silk, F.Cu at (51.6, 169.0)
- added D3001: White, mark:LED_0603_1608Metric_no_silk, F.Cu at (51.6, 179.5)
- added D3201: White, mark:LED_0603_1608Metric_no_silk, F.Cu at (68.0, 179.5)
- added D3301: White, mark:LED_0603_1608Metric_no_silk, F.Cu at (84.5, 158.4)
- added D3401: White, mark:LED_0603_1608Metric_no_silk, F.Cu at (51.6, 221.8)
- added D3501: White, mark:LED_0603_1608Metric_no_silk, F.Cu at (68.0, 200.7)
- added D3601: White, mark:LED_0603_1608Metric_no_silk, F.Cu at (51.6, 242.9)
- added D3701: White, mark:LED_0603_1608Metric_no_silk, F.Cu at (117.3, 158.4)
- added D3801: White, mark:LED_0603_1608Metric_no_silk, F.Cu at (84.5, 190.1)
- added D3901: White, mark:LED_0603_1608Metric_no_silk, F.Cu at (51.6, 200.7)
- added D4001: White, mark:LED_0603_1608Metric_no_silk, F.Cu at (51.6, 190.1)
- added D401: White, mark:LED_0603_1608Metric_no_silk, F.Cu at (100.9, 211.2)
- added D4301: White, mark:LED_0603_1608Metric_no_silk, F.Cu at (166.6, 179.5)
- added D4501: White, mark:LED_0603_1608Metric_no_silk, F.Cu at (183.0, 190.1)
- added D4601: White, mark:LED_0603_1608Metric_no_silk, F.Cu at (215.8, 158.4)
- added D4701: White, mark:LED_0603_1608Metric_no_silk, F.Cu at (166.6, 200.7)
- added D4801: White, mark:LED_0603_1608Metric_no_silk, F.Cu at (133.7, 232.3)
- added D4901: White, mark:LED_0603_1608Metric_no_silk, F.Cu at (199.4, 179.5)
- added D5001: White, mark:LED_0603_1608Metric_no_silk, F.Cu at (150.2, 221.8)
- added D5101: White, mark:LED_0603_1608Metric_no_silk, F.Cu at (117.3, 221.8)
- added D5201: White, mark:LED_0603_1608Metric_no_silk, F.Cu at (150.2, 211.2)
- added D5301: White, mark:LED_0603_1608Metric_no_silk, F.Cu at (84.5, 169.0)
- added D5501: White, mark:LED_0603_1608Metric_no_silk, F.Cu at (117.3, 232.3)
- added D5601: White, mark:LED_0603_1608Metric_no_silk, F.Cu at (183.0, 169.0)
- added D5701: White, mark:LED_0603_1608Metric_no_silk, F.Cu at (133.7, 221.8)
- added D5801: White, mark:LED_0603_1608Metric_no_silk, F.Cu at (150.2, 200.7)
- added D5901: White, mark:LED_0603_1608Metric_no_silk, F.Cu at (199.4, 158.4)
- added D6101: White, mark:LED_0603_1608Metric_no_silk, F.Cu at (133.7, 200.7)
- added D6201: White, mark:LED_0603_1608Metric_no_silk, F.Cu at (68.0, 242.9)
- added D6301: White, mark:LED_0603_1608Metric_no_silk, F.Cu at (183.0, 158.4)
- added D6401: White, mark:LED_0603_1608Metric_no_silk, F.Cu at (166.6, 169.0)
- added D6501: White, mark:LED_0603_1608Metric_no_silk, F.Cu at (100.9, 232.3)
- added D6701: White, mark:LED_0603_1608Metric_no_silk, F.Cu at (84.5, 179.5)
- added D6801: White, mark:LED_0603_1608Metric_no_silk, F.Cu at (51.6, 158.4)
- added D6901: White, mark:LED_0603_1608Metric_no_silk, F.Cu at (100.9, 169.0)
- added D7001: White, mark:LED_0603_1608Metric_no_silk, F.Cu at (68.0, 190.1)
- added D7101: White, mark:LED_0603_1608Metric_no_silk, F.Cu at (51.6, 211.2)
- added D7401: White, mark:LED_0603_1608Metric_no_silk, F.Cu at (117.3, 242.9)
- added D7501: White, mark:LED_0603_1608Metric_no_silk, F.Cu at (166.6, 190.1)
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- renumbered C14 to C101, C3 to C102, C4 to C103, C7 to C104, C8 to C105, C11 to C106, C12 to C107, C15 to C108, C16 to C109, H1 to H101, H2 to H102, H3 to H103, H4 to H104, H5 to H105, H6 to H106, H7 to H107, H8 to H108, J1 to J101, R4 to R101, R5 to R102, SW4 to SW1001, SW5 to SW1201, SW6 to SW1401, SW7 to SW1601, SW1 to SW301, SW2 to SW601, SW3 to SW801, U1 to U101, U2 to U102, U3 to U103, U4 to U104
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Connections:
- SW1001 pad 1: VDDF -> VDD
- SW1001 pad 2: /Toggle Button 4/T flip-flop/TOGGLE -> /Button OR_A/T flip-flop/TOGGLE
- SW1201 pad 1: VDDF -> VDD
- SW1201 pad 2: /Toggle Button 5/T flip-flop/TOGGLE -> /Button OR_B/T flip-flop/TOGGLE
- SW1401 pad 1: VDDF -> VDD
- SW1401 pad 2: /Toggle Button 6/T flip-flop/TOGGLE -> /Button XOR_A/T flip-flop/TOGGLE
- SW1601 pad 1: VDDF -> VDD
- SW1601 pad 2: /Toggle Button 7/T flip-flop/TOGGLE -> /Button XOR_B/T flip-flop/TOGGLE
- SW301 pad 1: VDDF -> VDD
- SW301 pad 2: /Toggle Button 1/T flip-flop/TOGGLE -> /Button NOT_A/T flip-flop/TOGGLE
- SW601 pad 1: VDDF -> VDD
- SW601 pad 2: /Toggle Button 2/T flip-flop/TOGGLE -> /Button AND_A/T flip-flop/TOGGLE
- SW801 pad 1: VDDF -> VDD
- SW801 pad 2: /Toggle Button 3/T flip-flop/TOGGLE -> /Button AND_B/T flip-flop/TOGGLE
- U103 pad 12: /OR_X -> /OR_Y
- U103 pad 13: /XOR_X -> /XOR_Y
- U103 pad 8: /NOT_X -> /NOT_Y
- U103 pad 9: /AND_X -> /AND_Y
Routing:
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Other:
- board text added: "2mm for placement rules and case"
- board text removed: "Routing is intentionally shit, so I can use unpopulated boards to study crosstalk"

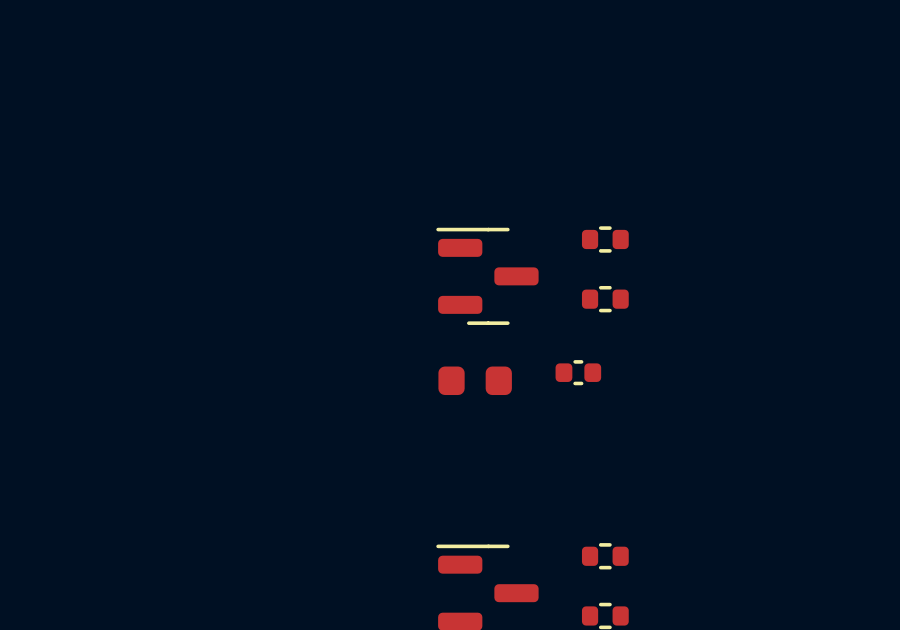
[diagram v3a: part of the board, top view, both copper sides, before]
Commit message: pcb-text plugin applied, next step is to write a replicate layout plugin that actually works
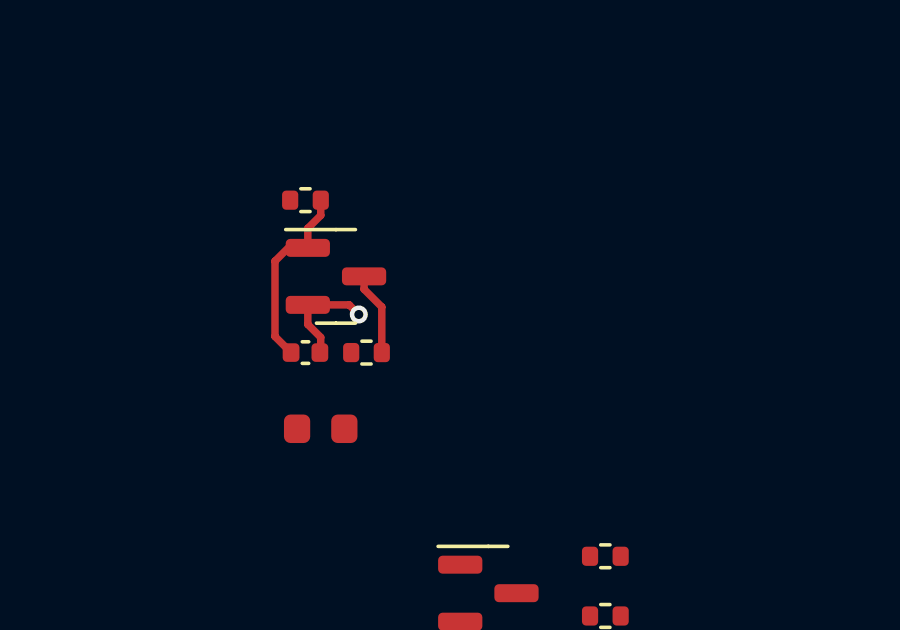
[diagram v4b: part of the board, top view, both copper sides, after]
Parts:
- C10001, C10101, C10201, C10301, C1701, C1801, C1901, C2001, C2101, C2201, C2301, C2401, C2501, C2601, C2701, C2801, C2901, C3001, C3201, C3301, C3401, C3501, C3601, C3701, C3801, C3901, C4001, C401, C4301, C4501, C4601, C4701, C4801, C4901, C5001, C5101, C5201, C5301, C5501, C5601, C5701, C5801, C5901, C6101, C6201, C6301, C6401, C6501, C6701, C6801, C6901, C7001, C7101, C7401, C7501, C7601, C7701, C7801, C8001, C8101, C8501, C8601, C8701, C8801, C8901, C9001, C9201, C9301, C9401, C9501, C9601, C9701, C9801, C9901: value 100n -> 1u
- R10001, R10101, R10201, R10301, R1701, R1801, R1901, R2001, R2101, R2201, R2301, R2401, R2501, R2601, R2701, R2801, R2901, R3001, R3201, R3301, R3401, R3501, R3601, R3701, R3801, R3901, R4001, R401, R4301, R4501, R4601, R4701, R4801, R4901, R5001, R5101, R5201, R5301, R5501, R5601, R5701, R5801, R5901, R6101, R6201, R6301, R6401, R6501, R6701, R6801, R6901, R7001, R7101, R7401, R7501, R7601, R7701, R7801, R8001, R8101, R8501, R8601, R8701, R8801, R8901, R9001, R9201, R9301, R9401, R9501, R9601, R9701, R9801, R9901: value 220k -> 100k
- moved R6801 10.1 mm to (46.0, 152.4)
- moved C6801 9.12 mm to (46.0, 157.5)
- moved R6802 8.16 mm to (48.0, 157.5)
- moved D6801 5.39 mm to (46.5, 160.0)
- moved Q6801 5.08 mm to (47.0, 154.9)
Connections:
- net /Button AND_A/VALUE renamed /BAA
- net /Button AND_B/VALUE renamed /BAB
- net /Button NOT_A/VALUE renamed /BNA
- net /Button OR_A/VALUE renamed /BOA
- net /Button OR_B/VALUE renamed /BOB
- net /Button XOR_A/VALUE renamed /BXA
- net /Button XOR_B/VALUE renamed /BXB
- net /Chain ALL_X/LED+delay 1/OUT renamed /Chain ALL_X/LINK1
- net /Chain ALL_X/LED+delay 2/OUT renamed /Chain ALL_X/LINK2
- net /Chain ALL_X/LED+delay 3/OUT renamed /Chain ALL_X/LINK3
- net /Chain ALL_X/LED+delay 4/OUT renamed /Chain ALL_X/LINK4
- net /Chain ALL_Y1/LED+delay 1/OUT renamed /Chain ALL_Y1/LINK1
- net /Chain ALL_Y1/LED+delay 2/OUT renamed /Chain ALL_Y1/LINK2
- net /Chain ALL_Y1/LED+delay 3/OUT renamed /Chain ALL_Y1/LINK3
- net /Chain ALL_Y1/LED+delay 4/OUT renamed /Chain ALL_Y1/LINK4
- net /Chain ALL_Y1/LED+delay 5/OUT renamed /Chain ALL_Y1/LINK5
- net /Chain ALL_Y1/OUT renamed /ALL_Z1
- net /Chain ALL_Y2/LED+delay 1/OUT renamed /Chain ALL_Y2/LINK1
- net /Chain ALL_Y2/LED+delay 2/OUT renamed /Chain ALL_Y2/LINK2
- net /Chain ALL_Y2/LED+delay 3/OUT renamed /Chain ALL_Y2/LINK3
- net /Chain ALL_Y2/LED+delay 4/OUT renamed /Chain ALL_Y2/LINK4
- net /Chain ALL_Y2/LED+delay 5/OUT renamed /Chain ALL_Y2/LINK5
- net /Chain ALL_Y2/OUT renamed /ALL_Z2
- net /Chain AND_A/LED+delay 1/OUT renamed /Chain AND_A/LINK1
- net /Chain AND_A/LED+delay 2/OUT renamed /Chain AND_A/LINK2
- net /Chain AND_A/LED+delay 3/OUT renamed /Chain AND_A/LINK3
- net /Chain AND_A/LED+delay 4/OUT renamed /Chain AND_A/LINK4
- net /Chain AND_B/LED+delay 1/OUT renamed /Chain AND_B/LINK1
- net /Chain AND_B/LED+delay 2/OUT renamed /Chain AND_B/LINK2
- net /Chain AND_B/LED+delay 3/OUT renamed /Chain AND_B/LINK3
- net /Chain AND_B/LED+delay 4/OUT renamed /Chain AND_B/LINK4
- net /Chain AND_X/LED+delay 1/OUT renamed /Chain AND_X/LINK1
- net /Chain AND_X/LED+delay 2/OUT renamed /Chain AND_X/LINK2
- net /Chain AND_X/LED+delay 3/OUT renamed /Chain AND_X/LINK3
- net /Chain AND_X/LED+delay 4/OUT renamed /Chain AND_X/LINK4
- net /Chain AND_X/LED+delay 5/OUT renamed /Chain AND_X/LINK5
- net /Chain NOT_A/LED+delay 1/OUT renamed /Chain NOT_A/LINK1
- net /Chain NOT_A/LED+delay 2/OUT renamed /Chain NOT_A/LINK2
- net /Chain NOT_A/LED+delay 3/OUT renamed /Chain NOT_A/LINK3
- net /Chain NOT_A/LED+delay 4/OUT renamed /Chain NOT_A/LINK4
- net /Chain NOT_X/LED+delay 1/OUT renamed /Chain NOT_X/LINK1
- net /Chain NOT_X/LED+delay 2/OUT renamed /Chain NOT_X/LINK2
- net /Chain NOT_X/LED+delay 3/OUT renamed /Chain NOT_X/LINK3
- net /Chain NOT_X/LED+delay 4/OUT renamed /Chain NOT_X/LINK4
- net /Chain NOT_X/LED+delay 5/OUT renamed /Chain NOT_X/LINK5
- net /Chain OR_A/LED+delay 1/OUT renamed /Chain OR_A/LINK1
- net /Chain OR_A/LED+delay 2/OUT renamed /Chain OR_A/LINK2
- net /Chain OR_A/LED+delay 3/OUT renamed /Chain OR_A/LINK3
- net /Chain OR_A/LED+delay 4/OUT renamed /Chain OR_A/LINK4
- net /Chain OR_B/LED+delay 1/OUT renamed /Chain OR_B/LINK1
- net /Chain OR_B/LED+delay 2/OUT renamed /Chain OR_B/LINK2
- net /Chain OR_B/LED+delay 3/OUT renamed /Chain OR_B/LINK3
- net /Chain OR_B/LED+delay 4/OUT renamed /Chain OR_B/LINK4
- net /Chain OR_X/LED+delay 1/OUT renamed /Chain OR_X/LINK1
- net /Chain OR_X/LED+delay 2/OUT renamed /Chain OR_X/LINK2
- net /Chain OR_X/LED+delay 3/OUT renamed /Chain OR_X/LINK3
- net /Chain OR_X/LED+delay 4/OUT renamed /Chain OR_X/LINK4
- net /Chain XOR_A/LED+delay 1/OUT renamed /Chain XOR_A/LINK1
- net /Chain XOR_A/LED+delay 2/OUT renamed /Chain XOR_A/LINK2
- net /Chain XOR_A/LED+delay 3/OUT renamed /Chain XOR_A/LINK3
- net /Chain XOR_A/LED+delay 4/OUT renamed /Chain XOR_A/LINK4
- net /Chain XOR_B/LED+delay 1/OUT renamed /Chain XOR_B/LINK1
- net /Chain XOR_B/LED+delay 2/OUT renamed /Chain XOR_B/LINK2
- net /Chain XOR_B/LED+delay 3/OUT renamed /Chain XOR_B/LINK3
- net /Chain XOR_B/LED+delay 4/OUT renamed /Chain XOR_B/LINK4
- net /Chain XOR_X/LED+delay 1/OUT renamed /Chain XOR_X/LINK1
- net /Chain XOR_X/LED+delay 2/OUT renamed /Chain XOR_X/LINK2
- net /Chain XOR_X/LED+delay 3/OUT renamed /Chain XOR_X/LINK3
- net /Chain XOR_X/LED+delay 4/OUT renamed /Chain XOR_X/LINK4
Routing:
- net /Chain AND_A/LINK3: track 0.00 -> 6.37 mm
- net VSS: track 102.1 -> 105.7 mm, vias 33 -> 34
- net Net-(Q6801-Pad3): track 0.00 -> 2.78 mm
